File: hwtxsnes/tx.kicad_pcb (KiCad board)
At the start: 2 copper layers, 125.7 x 45 mm, 44 parts, among them IC1 ATMEGA328-A, J1 POWER_JACK, P1 nRF, P2 ISP, P3 bLT+, P4 bLT-, P5 bRT+, P6 bRT-, P7 SER_RX, P8 SER_TX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

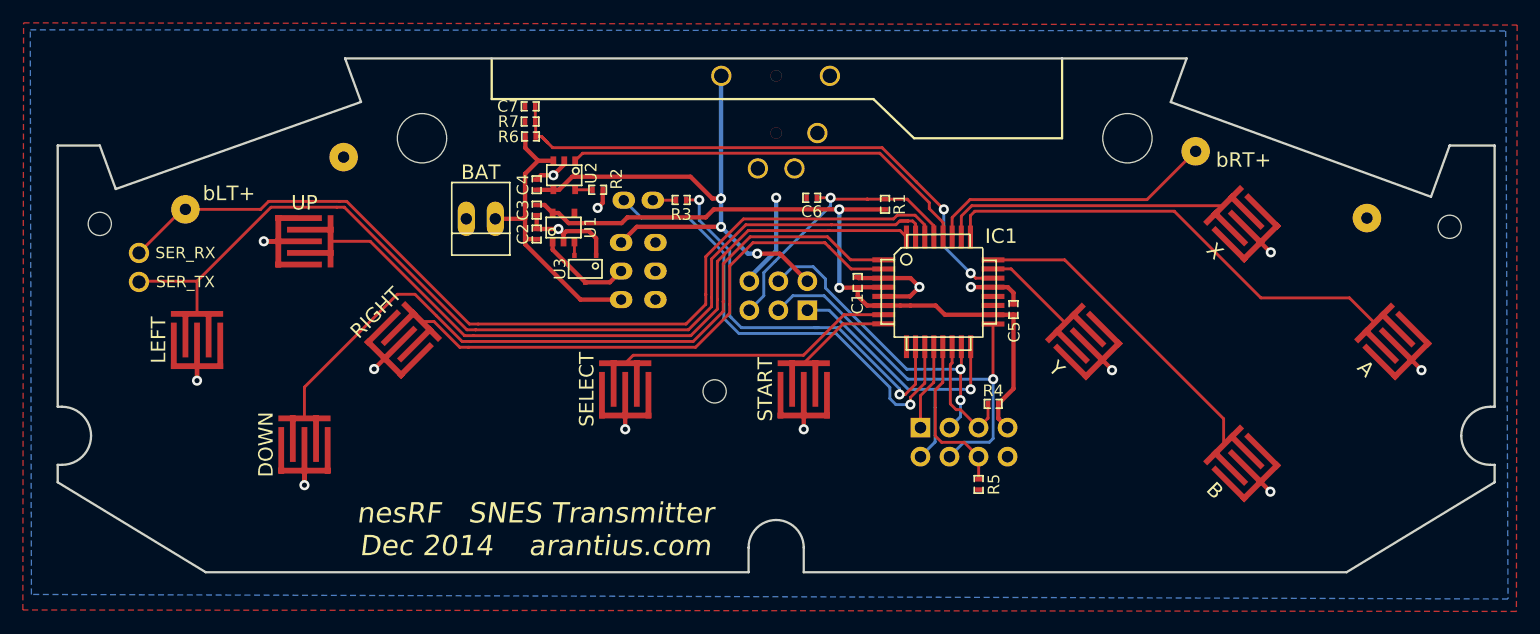
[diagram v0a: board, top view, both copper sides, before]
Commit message: v2
* Schematic revs:
  * TVS protection on TX
  * TX voltage divider moved after the power switch
  * RX adds crystal to run at 16MHz
RX software tested w/ a real console.
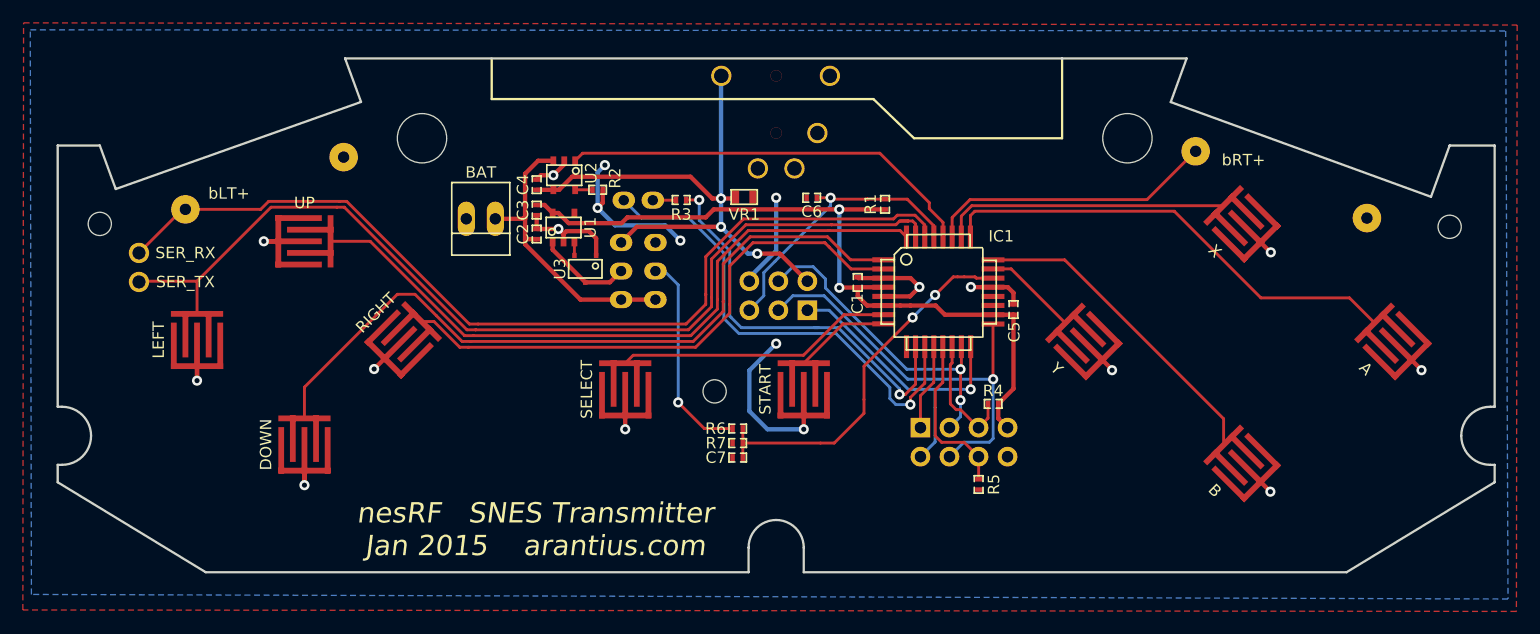
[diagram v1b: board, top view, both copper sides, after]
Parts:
- added VR1: VR, SMD_Packages:SMD-0603, F.Cu at (85.5, 37.5)
- moved C7 35.7 mm to (84.9, 60.3)
- moved R7 33.5 mm to (84.9, 59.1)
- moved R6 31.3 mm to (84.9, 57.8)
- turned C4 to 90 degrees
- turned R1 to 270 degrees
- turned R2 to 180 degrees
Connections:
- net /DIV_BAT renamed /DIV_BAT_OUT
- C4 pad 1: GND -> +5V
- C4 pad 2: +5V -> GND
- IC1 pad 19: Net-(IC1-Pad19) -> (no net)
- IC1 pad 20: Net-(IC1-Pad20) -> (no net)
- IC1 pad 9: Net-(IC1-Pad9) -> (no net)
- J1 pad 2: Net-(J1-Pad2) -> (no net)
- J1 pad 3: Net-(J1-Pad3) -> (no net)
- R1 pad 1: /VCC -> /~RST
- R1 pad 2: /~RST -> /VCC
- R2 pad 1: Net-(R2-Pad1) -> GND
- R2 pad 2: GND -> Net-(R2-Pad2)
- R6 pad 2: /RAW_BATT -> /DIV_BAT_IN
- SW1 pad 4: Net-(SW1-Pad4) -> (no net)
- SW1 pad 5: Net-(SW1-Pad5) -> /DIV_BAT_IN
- SW1 pad 6: Net-(SW1-Pad6) -> /RAW_BATT
- U1 pad 4: Net-(U1-Pad4) -> (no net)
- U2 pad 5: Net-(R2-Pad1) -> Net-(R2-Pad2)
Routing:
- net GND: track 76.3 -> 104.8 mm, vias 16 -> 19
- net /DIV_BAT_IN: track 0.00 -> 18.5 mm, vias 0 -> 1
- net /DIV_BAT_OUT: track 50.5 -> 32.9 mm
- net Net-(R2-Pad2): track 0.00 -> 1.52 mm
- net Net-(R2-Pad1): track 1.52 -> 0.00 mm
- net +5V: track 50.2 -> 51.6 mm
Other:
- board text added: "nesRF SNES Transmitter Jan 2015 arantius.com"
- board text removed: "nesRF SNES Transmitter Dec 2014 arantius.com"

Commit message: end-to-end working on breadboard
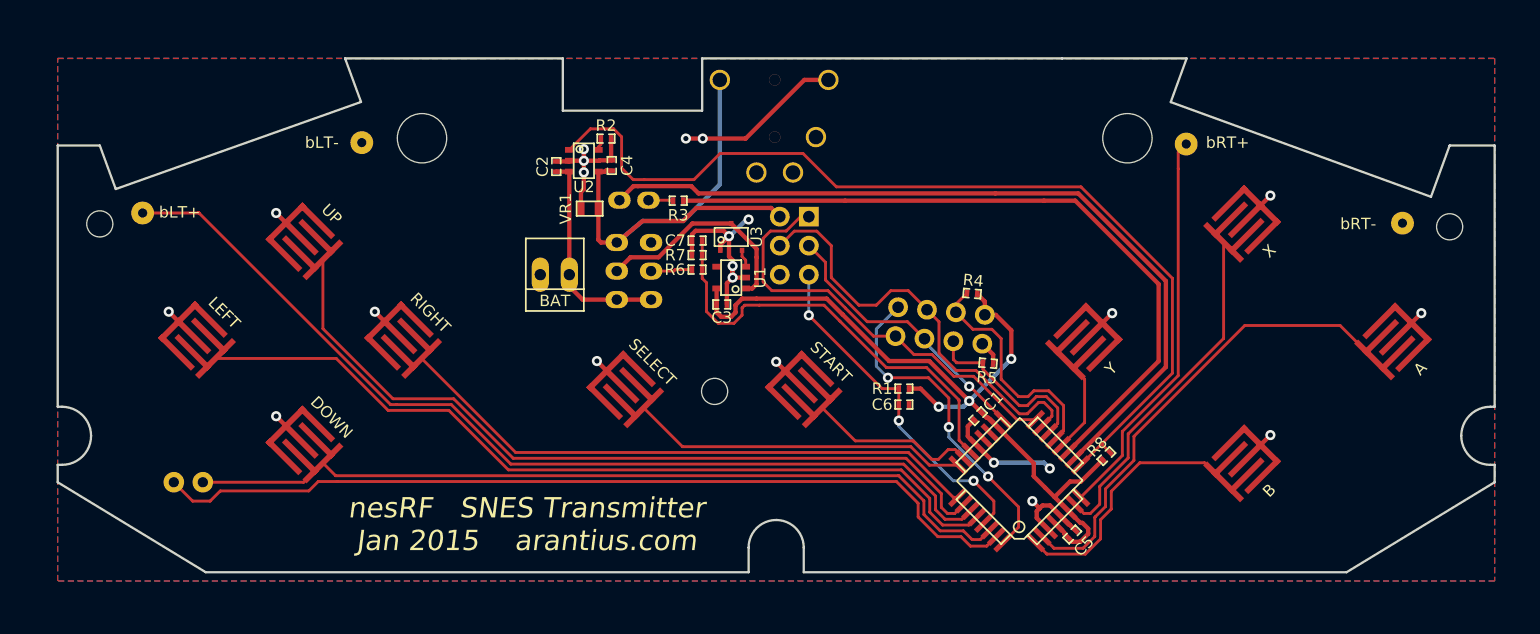
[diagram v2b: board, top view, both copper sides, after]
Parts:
- added R8: 10k, SMD_Packages:SMD-0402_r, F.Cu at (117.2, 60.2)
- P1: footprint Pin_Headers:Pin_Header_Straight_2x04 -> nRF_Header_2x04
- P3, P4, P5, P6: footprint Wire_Pads:SolderWirePad_single_1mmDrill -> Wire_Pads:SolderWirePad_single_0-8mmDrill
- P7, P8: footprint Wire_Pads:SolderWirePad_single_1mmDrill -> Wire_Pads:SolderWirePad_single_0-8mmDrill; moved to B.Cu
- R2: value 24.9k -> 19.1k
- U2: value MCP73831 -> MCP73832
- moved P7 20.8 mm to (38.1, 62.5), turned to 0 degrees
- moved C5 20.3 mm to (114.2, 67.1), turned to 45 degrees
- moved C6 19.8 mm to (99.4, 55.7), turned to 180 degrees
- moved C7 19.3 mm to (81.3, 41.3)
- moved C3 18.2 mm to (83.5, 46.9), turned to 0 degrees
- moved IC1 18.0 mm to (109.5, 62.4), turned to 135 degrees
- moved P8 17.8 mm to (35.6, 62.5), turned to 0 degrees
- moved R7 16.8 mm to (81.3, 42.6)
- moved R1 16.2 mm to (99.4, 54.3), turned to 0 degrees
- moved C1 15.7 mm to (105.9, 56.7), turned to 225 degrees
- moved U1 15.3 mm to (84.3, 44.6), turned to 90 degrees
- moved R6 14.4 mm to (81.3, 43.9)
- moved VR1 13.6 mm to (71.9, 38.5), turned to 180 degrees
- moved U3 13.1 mm to (84.3, 41.0), turned to 0 degrees
- moved R5 10.6 mm to (106.8, 52.1), turned to 355 degrees
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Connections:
- net Net-(R2-Pad2) renamed /CHRG_PROG
- net Net-(R3-Pad1) renamed /LED_LIMITER
- IC1 pad 1: /bDOWN -> /bB
- IC1 pad 10: /LED- -> /LED+
- IC1 pad 11: /LED+ -> /LED-
- IC1 pad 12: /RF_IRQ -> /bY
- IC1 pad 13: /RF_CE -> /RF_CSN
- IC1 pad 14: /RF_CSN -> /RF_CE
- IC1 pad 2: /bRIGHT -> /bA
- IC1 pad 23: /bY -> /bSTART
- IC1 pad 24: /bB -> /bSELECT
- IC1 pad 25: /bA -> /bRIGHT
- IC1 pad 26: /bX -> /bUP
- IC1 pad 27: /bRT -> /bLT
- IC1 pad 28: /CHRG_STAT -> /bLEFT
- IC1 pad 30: /bLT -> /bDOWN
- IC1 pad 31: /bLEFT -> /TX
- IC1 pad 32: /bUP -> /RF_IRQ
- IC1 pad 7: /bSELECT -> /bX
- IC1 pad 8: /bSTART -> /bRT
- IC1 pad 9: (no net) -> /CHRG_STAT
- P7 pad 1: /bLT -> /bDOWN
- P8 pad 1: /bLEFT -> /TX
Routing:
- net /TX: track 0.00 -> 76.8 mm
- net /CHRG_STAT: track 36.6 -> 83.1 mm
- net /LED+: track 42.0 -> 70.6 mm, vias 1 -> 0
- net GND: track 104.8 -> 77.6 mm, vias 19 -> 22
- net /LED-: track 35.8 -> 62.6 mm, vias 2 -> 0
- net /RF_IRQ: track 7.57 -> 29.2 mm, vias 0 -> 3
- net /DIV_BAT_IN: track 18.5 -> 3.63 mm, vias 1 -> 0
- net /SCK: track 36.9 -> 24.4 mm
- net /bLEFT: track 91.9 -> 80.7 mm
- net /SW_BATT: track 8.25 -> 19.1 mm
- net /MISO: track 27.4 -> 37.4 mm, vias 1 -> 0
- net /RF_CSN: track 10.8 -> 20.6 mm
- net /MOSI: track 28.2 -> 37.7 mm, vias 2 -> 0
- net /bRT: track 25.4 -> 34.7 mm
- net /bUP: track 66.0 -> 75.3 mm
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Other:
- outline, holes or cut-outs redrawn
- net class Default: clearance 0.2286 -> 0.254
- rule trace_clearance: 0.2286 -> 0.254
